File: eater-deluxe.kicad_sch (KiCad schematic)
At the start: 0 parts

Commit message: Schematic: All special components added
All special components, that are somewhat special has been added. These
are things like the crystal oscillator, the cpu, via, sram, eeprom, etc.

Signed-off-by: Lucy <user@domain.tld>
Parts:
- added U1: 6502, Package_DIP:DIP-40_W15.24mm_Socket, symbol PCM_65xx-library:6502
- added U2: W65C22NxP, Package_DIP:DIP-40_W15.24mm_Socket, symbol PCM_65xx-library:W65C22NxP
- added U3: W65C51NxP, Package_DIP:DIP-28_W15.24mm_Socket, symbol PCM_65xx-library:W65C51NxP
- added U4: 28C256, Package_DIP:DIP-28_W15.24mm_Socket, symbol Memory_EEPROM:28C256
- added U5: HM62256BLP, Package_DIP:DIP-28_W15.24mm_Socket, symbol Memory_RAM:HM62256BLP
- added U6: CD74HC00E, CD74HC00E:N14, symbol 2026-05-30_09-57-03:CD74HC00E
- added U7: MXO45-3C-1M000000, MXO45_3C_1M000000:DIP4_MXO45-3C-1M000000_CTS, symbol 2026-05-30_10-11-52:MXO45-3C-1M000000
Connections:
- new net: U1.1 (VSS), U1.21 (VSS)
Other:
- title: (none) -> ${TITLE}

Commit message: Schematics. Intermediate commit: only W65C22 Missing
Signed-off-by: Lucy <user@domain.tld>
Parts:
- added C10, C13, C16, C17, C5, C6, C7, C8, C9: 0.1uF, Capacitor_THT:C_Axial_L12.0mm_D6.5mm_P15.00mm_Horizontal, symbol Device:C
- added C11, C12, C14, C15: 1uF, Capacitor_THT:C_Axial_L12.0mm_D6.5mm_P15.00mm_Horizontal, symbol Device:C
- added D1: SB140, Diode_THT:D_DO-41_SOD81_P10.16mm_Horizontal, symbol Diode:SB140
- added J1: PJ-202A, PJ-202A:CUI_PJ-202A, symbol PJ-202A:PJ-202A
- added J2: DE9_Socket, Connector_Dsub:DSUB-9_Socket_Horizontal_P2.77x2.54mm_EdgePinOffset9.40mm, symbol Connector:DE9_Socket
- added R1, R2: 1k, Resistor_THT:R_Axial_DIN0204_L3.6mm_D1.6mm_P7.62mm_Horizontal, symbol Device:R
- added SW1: RESET, Button_Switch_THT:SW_PUSH-12mm, symbol Switch:SW_Push
- added U7: MAX232, Package_DIP:DIP-16_W7.62mm_Socket, symbol Interface_UART:MAX232
- renumbered U7 to X1
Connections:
- net GND: now reaches U3.1 (VSS)
- net GND: now also U1.1 (VSS), U1.21 (VSS), U4.14 (GND), U4.22 (~{OE}), U5.14 (GND), U6.7 (GND), X1.4, C10.2, C13.2, C14.2, C15.2, C16.2, C17.1, C5.1, C6.1, C7.2, C8.2, C9.2, J1.2, J2.5, SW1.1, U7.15 (GND)
- net TxD: now reaches U3.10 (TxD)
- net TxD: now also U7.11 (T1IN)
- net RxD: now reaches U3.12 (RxD)
- net RxD: now also U7.12 (R1OUT)
- net a0: now reaches U3.13 (RS0)
- net a0: now also U1.9 (A0), U2.38 (RS0), U4.10 (A0), U5.10 (A0)
- net a1: now reaches U3.14 (RS1)
- net a1: now also U1.10 (A1), U2.37 (RS1), U4.9 (A1), U5.9 (A1)
- net +5V: now reaches U3.15 (VCC)
- net +5V: now also U1.25 (A15), U1.36 (BE), U1.6 (~{NMI}), U1.8 (VCC), U4.27 (~{WE}), U4.28 (VCC), U5.28 (VCC), U6.1 (1A), U6.14 (VCC), U6.2 (1B), X1.1, X1.3, C10.1, C13.1, C16.1, C17.2, C6.2, C7.1, C8.1, C9.1, J1.1, R1.1, R2.1, U7.16 (VCC)
- net d0: now reaches U3.18 (D0)
- net d0: now also U1.33 (D0), U2.33 (D0), U4.11 (D0), U5.11 (Q0)
- net d1: now reaches U3.19 (D1)
- net d1: now also U1.32 (D1), U2.32 (D1), U4.12 (D1), U5.12 (Q1)
- net a12: now reaches U3.2 (CS1)
- net a12: now also U1.22 (A12), U4.2 (A12), U5.2 (A12)
- net d2: now reaches U3.20 (D2)
- net d2: now also U1.31 (D2), U2.31 (D2), U4.13 (D2), U5.13 (Q2)
- net d3: now reaches U3.21 (D3)
- net d3: now also U1.30 (D3), U2.30 (D3), U4.15 (D3), U5.15 (Q3)
- net d4: now reaches U3.22 (D4)
- net d4: now also U1.29 (D4), U2.29 (D4), U4.16 (D4), U5.16 (Q4)
- net d5: now reaches U3.23 (D5)
- net d5: now also U1.28 (D5), U2.28 (D5), U4.17 (D5), U5.17 (Q5)
- net d6: now reaches U3.24 (D6)
- net d6: now also U1.27 (D6), U2.27 (D6), U4.18 (D6), U5.18 (Q6)
- net d7: now reaches U3.25 (D7)
- net d7: now also U1.26 (D7), U2.26 (D7), U4.19 (D7), U5.19 (Q7)
- net at U3.26 (~{IRQ}): now also D1.1 (K)
- net CLK: now reaches U3.27 (ϕ2)
- net CLK: now also U1.37 (ϕ0), U2.25 (ϕ2), U6.5 (2B), X1.2
- net RW: now reaches U3.28 (R/~{W})
- net RW: now also U1.34 (R/~{W}), U2.22 (R/~{W}), U5.27 (~{WE})
- net CS2: now reaches U3.3 (~{CS2})
- net CS2: now also U2.23 (~{CS2}), U6.8 (3Y)
- net RESET: now reaches U3.4 (~{RES})
- net RESET: now also U1.40 (~{RES}), U2.34 (~{RES}), C5.2, R1.2, SW1.2
- net a14: now reaches U5.1 (A14)
- net a14: now also U1.24 (A14), U4.1 (A14), U5.22 (~{OE}), U6.10 (3B)
- net 62256_CS: now reaches U5.20 (~{CS})
- net 62256_CS: now also U6.6 (2Y)
- net a10: now reaches U5.21 (A10)
- net a10: now also U1.19 (A10), U4.21 (A10)
- net a11: now reaches U5.23 (A11)
- net a11: now also U1.20 (A11), U4.23 (A11)
- net a9: now reaches U5.24 (A9)
- net a9: now also U1.18 (A9), U4.24 (A9)
- net a8: now reaches U5.25 (A8)
- net a8: now also U1.17 (A8), U4.25 (A8)
- net a13: now reaches U5.26 (A13)
- net a13: now also U1.23 (A13), U4.26 (A13)
- net a7: now reaches U5.3 (A7)
- net a7: now also U1.16 (A7), U4.3 (A7)
- net a6: now reaches U5.4 (A6)
- net a6: now also U1.15 (A6), U4.4 (A6)
- net a5: now reaches U5.5 (A5)
- net a5: now also U1.14 (A5), U4.5 (A5)
- net a4: now reaches U5.6 (A4)
- net a4: now also U1.13 (A4), U4.6 (A4)
- net a3: now reaches U5.7 (A3)
- net a3: now also U1.12 (A3), U2.35 (RS3), U4.7 (A3)
- net a2: now reaches U5.8 (A2)
- net a2: now also U1.11 (A2), U2.36 (RS2), U4.8 (A2)
- net 28c256_CS: now reaches U4.20 (~{CS})
- net 28c256_CS: now also U6.3 (1Y), U6.4 (2A), U6.9 (3A)
- net at U1.2 (RDY): now also R2.2
- net IRQ: now reaches U1.4 (~{IRQ})
- net IRQ: now also D1.2 (A)
- new net: J2.2, U7.14 (T1OUT)
- new net: J2.3, U7.13 (R1IN)
- new net: C14.1, U7.2 (VS+)
- new net: C11.1, U7.1 (C1+)
- new net: C11.2, U7.3 (C1-)
- new net: C15.1, U7.6 (VS-)
- new net: C12.1, U7.4 (C2+)
- new net: C12.2, U7.5 (C2-)
- no-connect marks 0 -> 18
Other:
- note added: "1MHz Computer Clock"
- note added: "ACIA"
- note added: "Barrel-Jack 5V In"
- note added: "CPU"
- note added: "EEPROM"
- note added: "RS232 UART TRANSCIEVER"
- note added: "Reset Switch"
- note added: "Serial"
- moved on the sheet: U2, U3, U4, U5, U6, X1

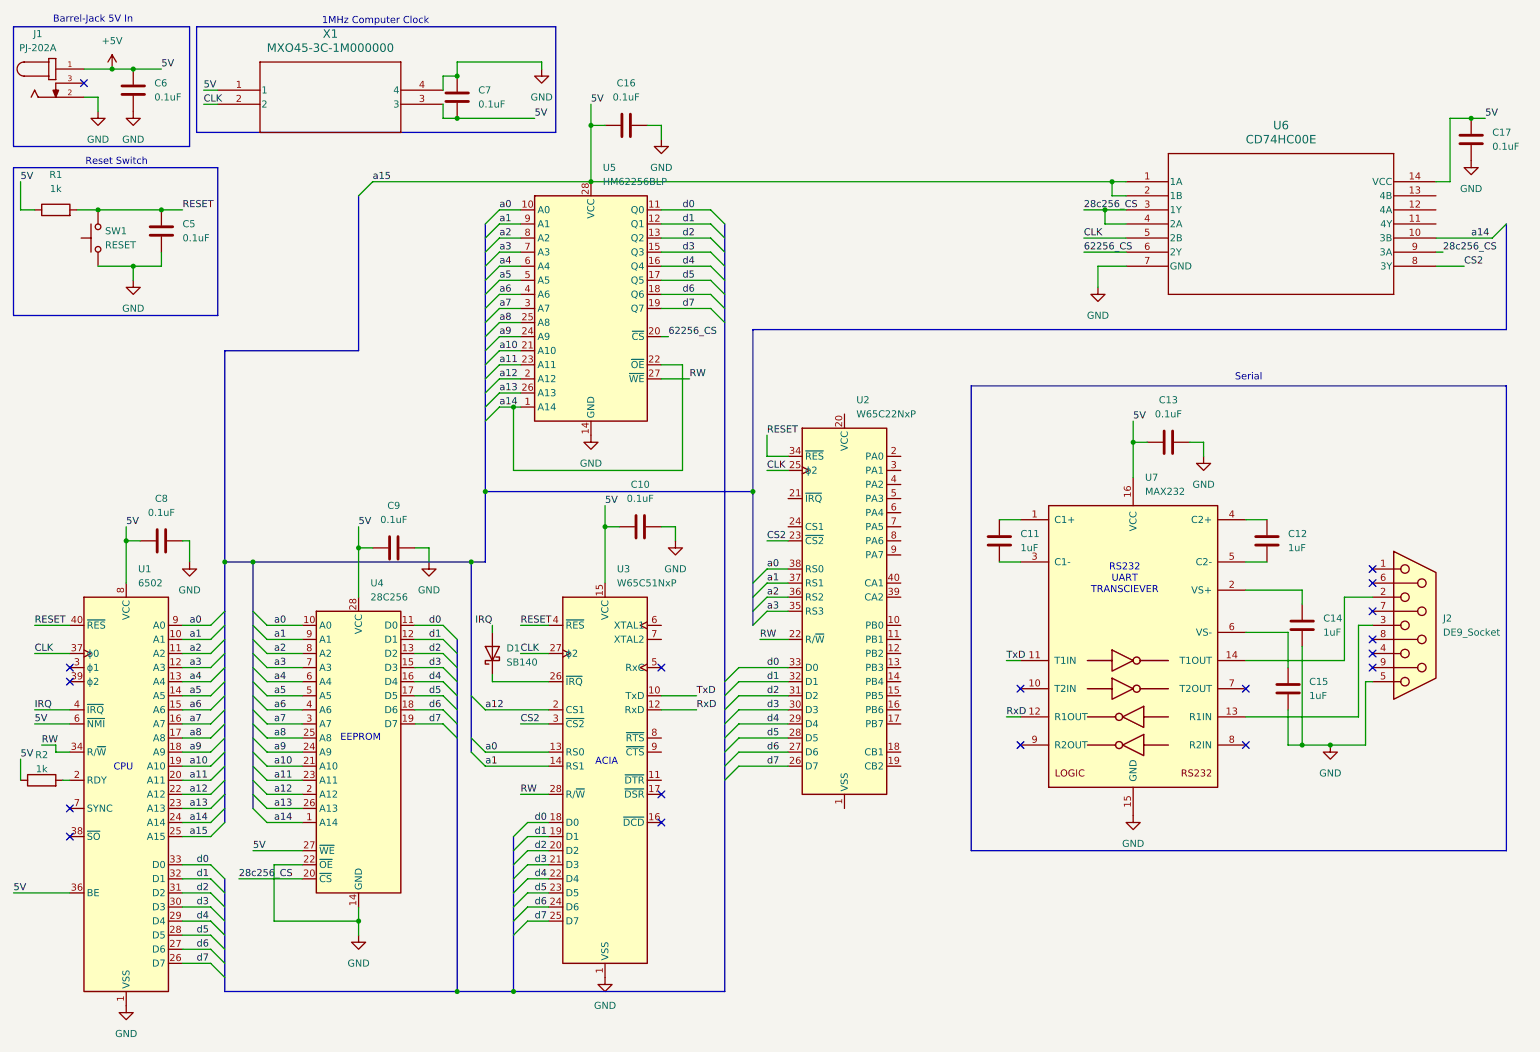
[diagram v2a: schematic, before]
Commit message: Schematics rev 1.0 finished
Signed-off-by: Lucy <user@domain.tld>
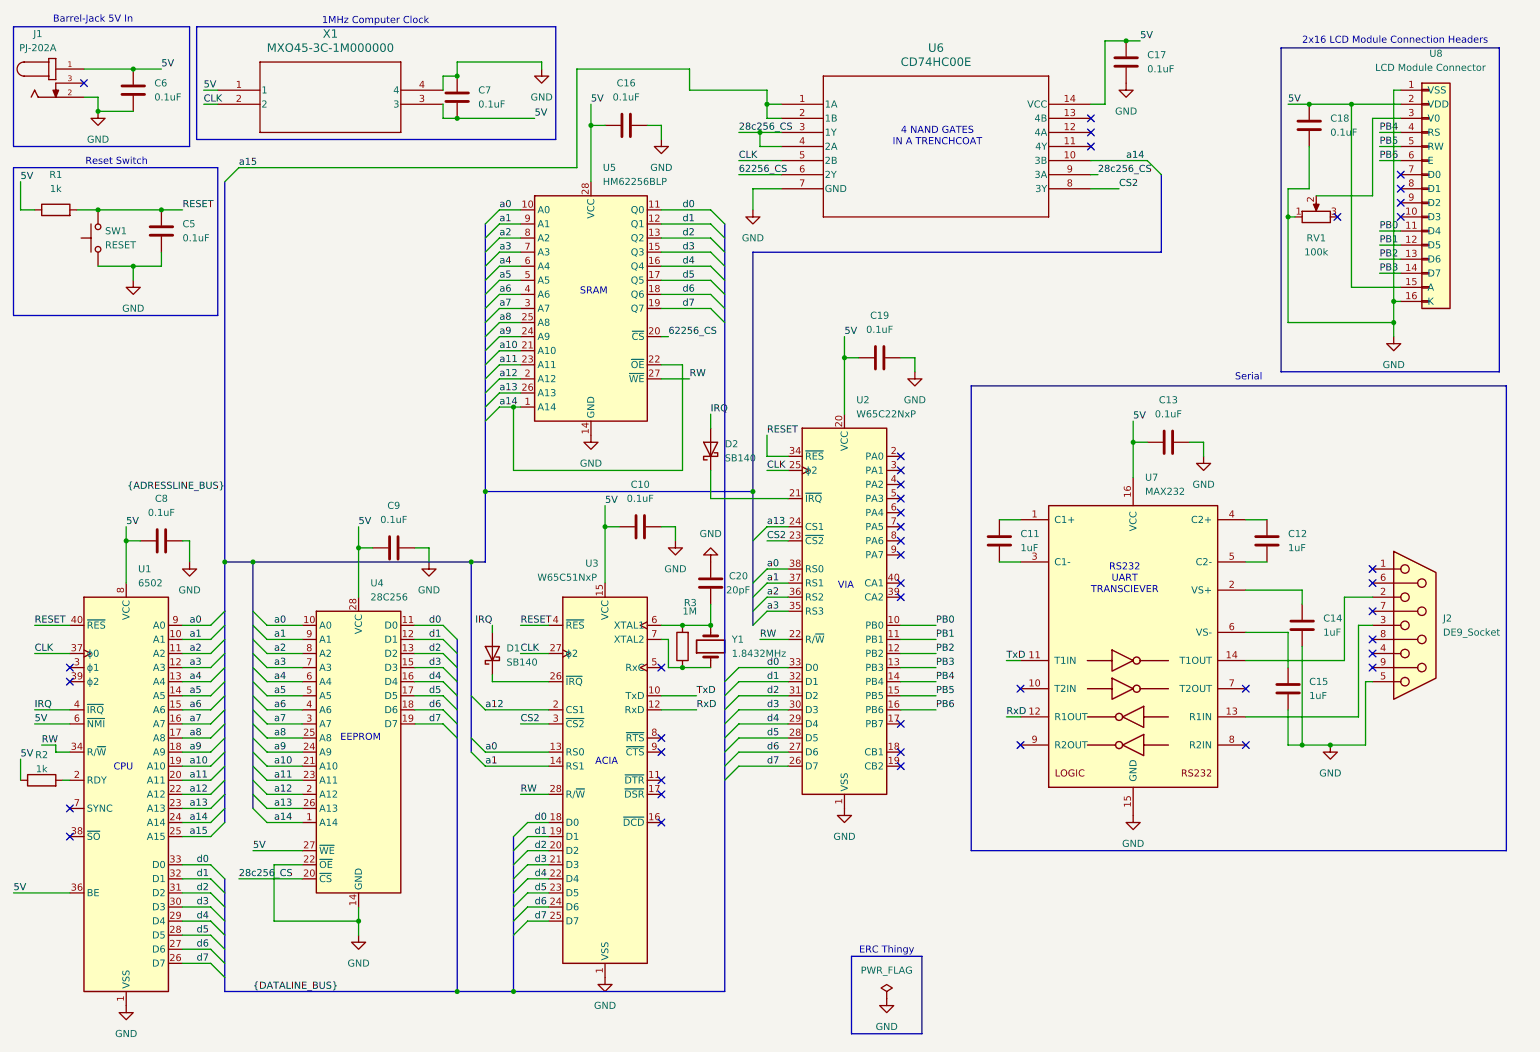
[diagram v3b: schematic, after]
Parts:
- added C18, C19: 0.1uF, Capacitor_THT:C_Axial_L12.0mm_D6.5mm_P15.00mm_Horizontal, symbol Device:C
- added C20: 20pF, Capacitor_THT:C_Axial_L12.0mm_D6.5mm_P15.00mm_Horizontal, symbol Device:C
- added D2: SB140, Diode_THT:D_DO-41_SOD81_P10.16mm_Horizontal, symbol Diode:SB140
- added R3: 1M, Resistor_THT:R_Axial_DIN0204_L3.6mm_D1.6mm_P7.62mm_Horizontal, symbol Device:R
- added RV1: 100k, Potentiometer_THT:Potentiometer_ACP_CA14-H2,5_Horizontal, symbol Device:R_Potentiometer
- added U8: LCD Module Connector, Connector_PinHeader_1.00mm:PinHeader_1x16_P1.00mm_Horizontal, symbol Connector_Generic:Conn_01x16
- added Y1: 1.8432MHz, Crystal:Crystal_HC49-U_Vertical, symbol Device:Crystal
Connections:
- net GND: now also U2.1 (VSS), C18.1, C19.2, C20.2, RV1.1, U8.1 (VSS), U8.16 (K)
- net IRQ: now also D2.2 (A)
- net a13: now also U2.24 (CS1)
- net at U3.6 (XTAL1): now also C20.1, R3.2, Y1.2
- net at U3.7 (XTAL2): now also R3.1, Y1.1
- net PB0: now reaches U2.10 (PB0)
- net PB0: now also U8.11 (D4)
- net PB1: now reaches U2.11 (PB1)
- net PB1: now also U8.12 (D5)
- net PB2: now reaches U2.12 (PB2)
- net PB2: now also U8.13 (D6)
- net PB3: now reaches U2.13 (PB3)
- net PB3: now also U8.14 (D7)
- net PB4: now reaches U2.14 (PB4)
- net PB4: now also U8.4 (RS)
- net PB5: now reaches U2.15 (PB5)
- net PB5: now also U8.5 (RW)
- net PB6: now reaches U2.16 (PB6)
- net PB6: now also U8.6 (E)
- net 5V: now reaches U2.20 (VCC)
- net 5V: now also C10.1, C13.1, C16.1, C17.2, C6.2, C7.1, C8.1, C9.1, J1.1, R1.1, R2.1, U1.36 (BE), U1.6 (~{NMI}), U1.8 (VCC), U3.15 (VCC), U4.27 (~{WE}), U4.28 (VCC), U5.28 (VCC), U6.14 (VCC), U7.16 (VCC), X1.1, X1.3, C18.2, C19.1, U8.15 (A), U8.2 (VDD)
- net at U2.21 (~{IRQ}): now also D2.1 (K)
- removed net +5V: C10.1, C13.1, C16.1, C17.2, C6.2, C7.1, C8.1, C9.1, J1.1, R1.1, R2.1, U1.25 (A15), U1.36 (BE), U1.6 (~{NMI}), U1.8 (VCC), U3.15 (VCC), U4.27 (~{WE}), U4.28 (VCC), U5.28 (VCC), U6.1 (1A), U6.14 (VCC), U6.2 (1B), U7.16 (VCC), X1.1, X1.3
- new net: RV1.2, U8.3 (V0)
- new net a15: U1.25 (A15), U6.1 (1A), U6.2 (1B)
- no-connect marks 18 -> 42
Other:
- note added: "2x16 LCD Module Connection Headers"
- note added: "4 NAND GATES IN A TRENCHCOAT"
- note added: "ERC Thingy"
- note added: "SRAM"
- note added: "VIA"
- moved on the sheet: C17, U6

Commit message: PCB Layout rev1.0 finished
Signed-off-by: Lucy <user@domain.tld>
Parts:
- added H1, H2, H3, H4: MountingHole, MountingHole:MountingHole_3.2mm_M3, symbol Mechanical:MountingHole
